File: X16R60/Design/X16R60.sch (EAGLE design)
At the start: 64 parts, among them J1 SMD Grove, K1 SMD Button Top, P1 HEXABIT__LED_MATRIX, Q1 2N7002, Q2 2N7002, SW1 LSM7-644C, U1 STM32F103C8T6, U2 XC6206P332MR, X2 8MHz

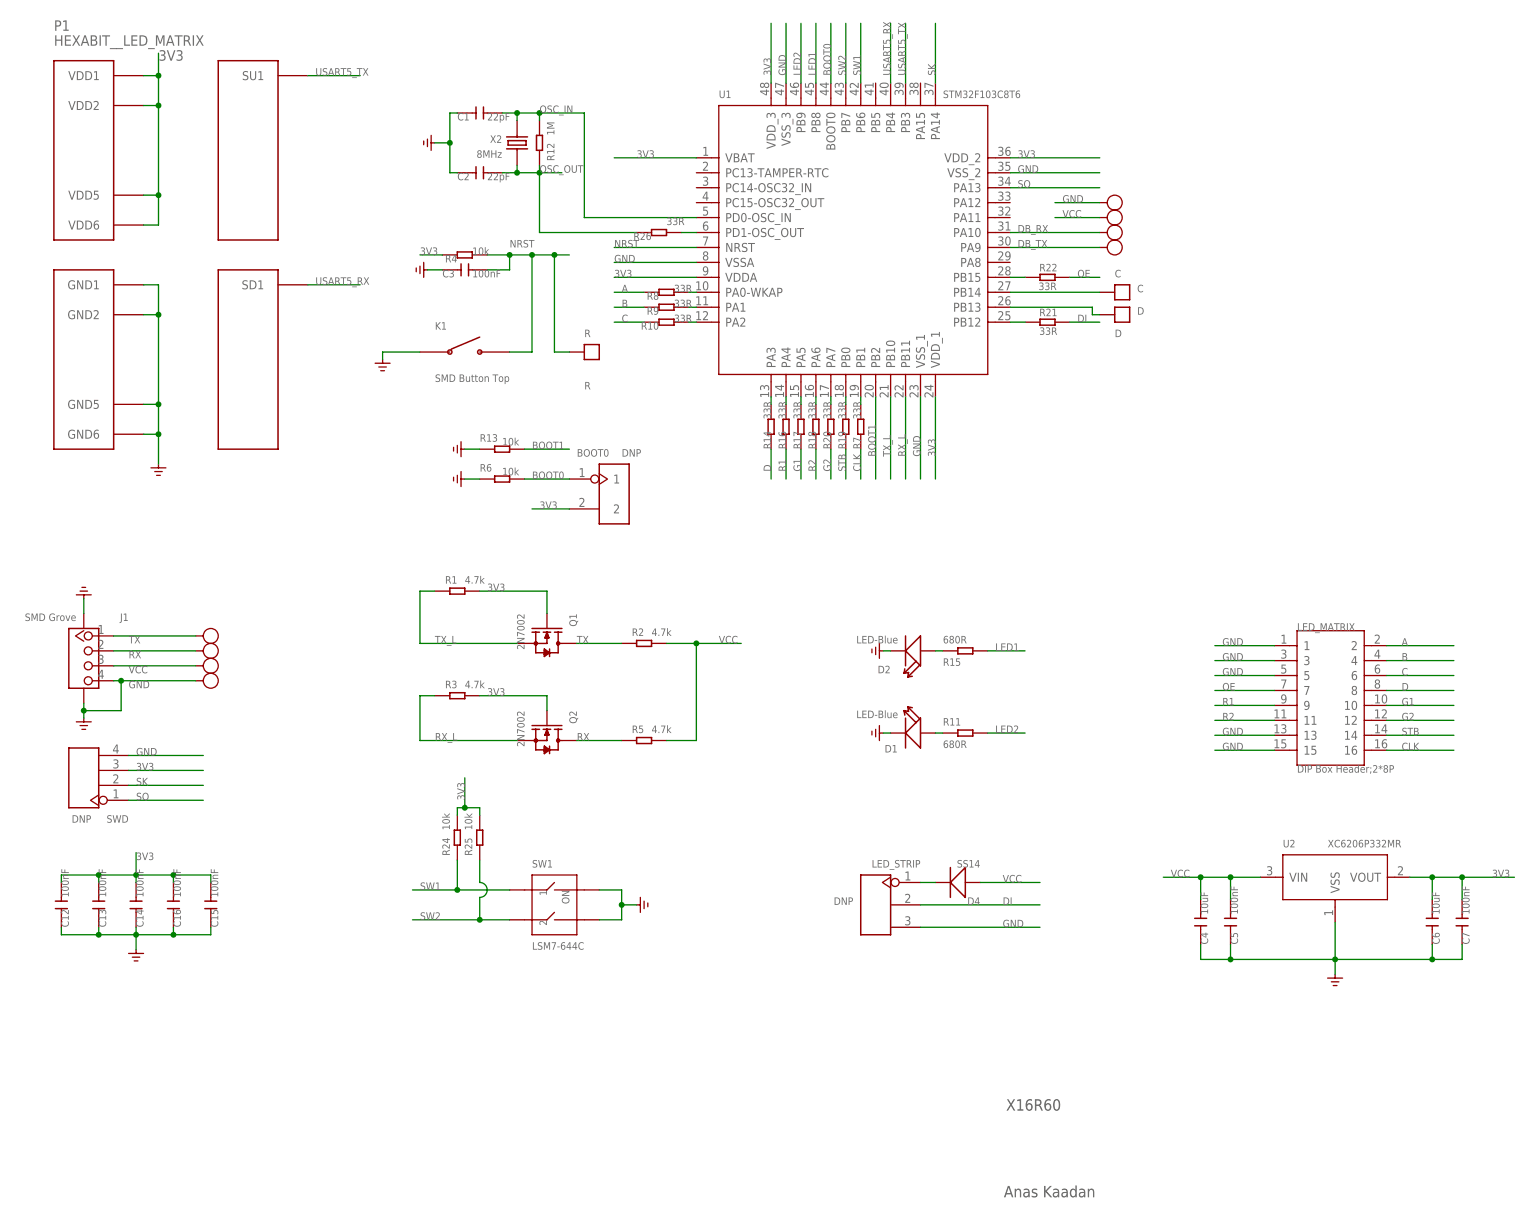
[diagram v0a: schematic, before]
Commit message: - Changed MCU.. - Deleted unnecessary components.. - Regenerated output files.. - Updated BOM.. - Updated Batch_4_21 on google docs..
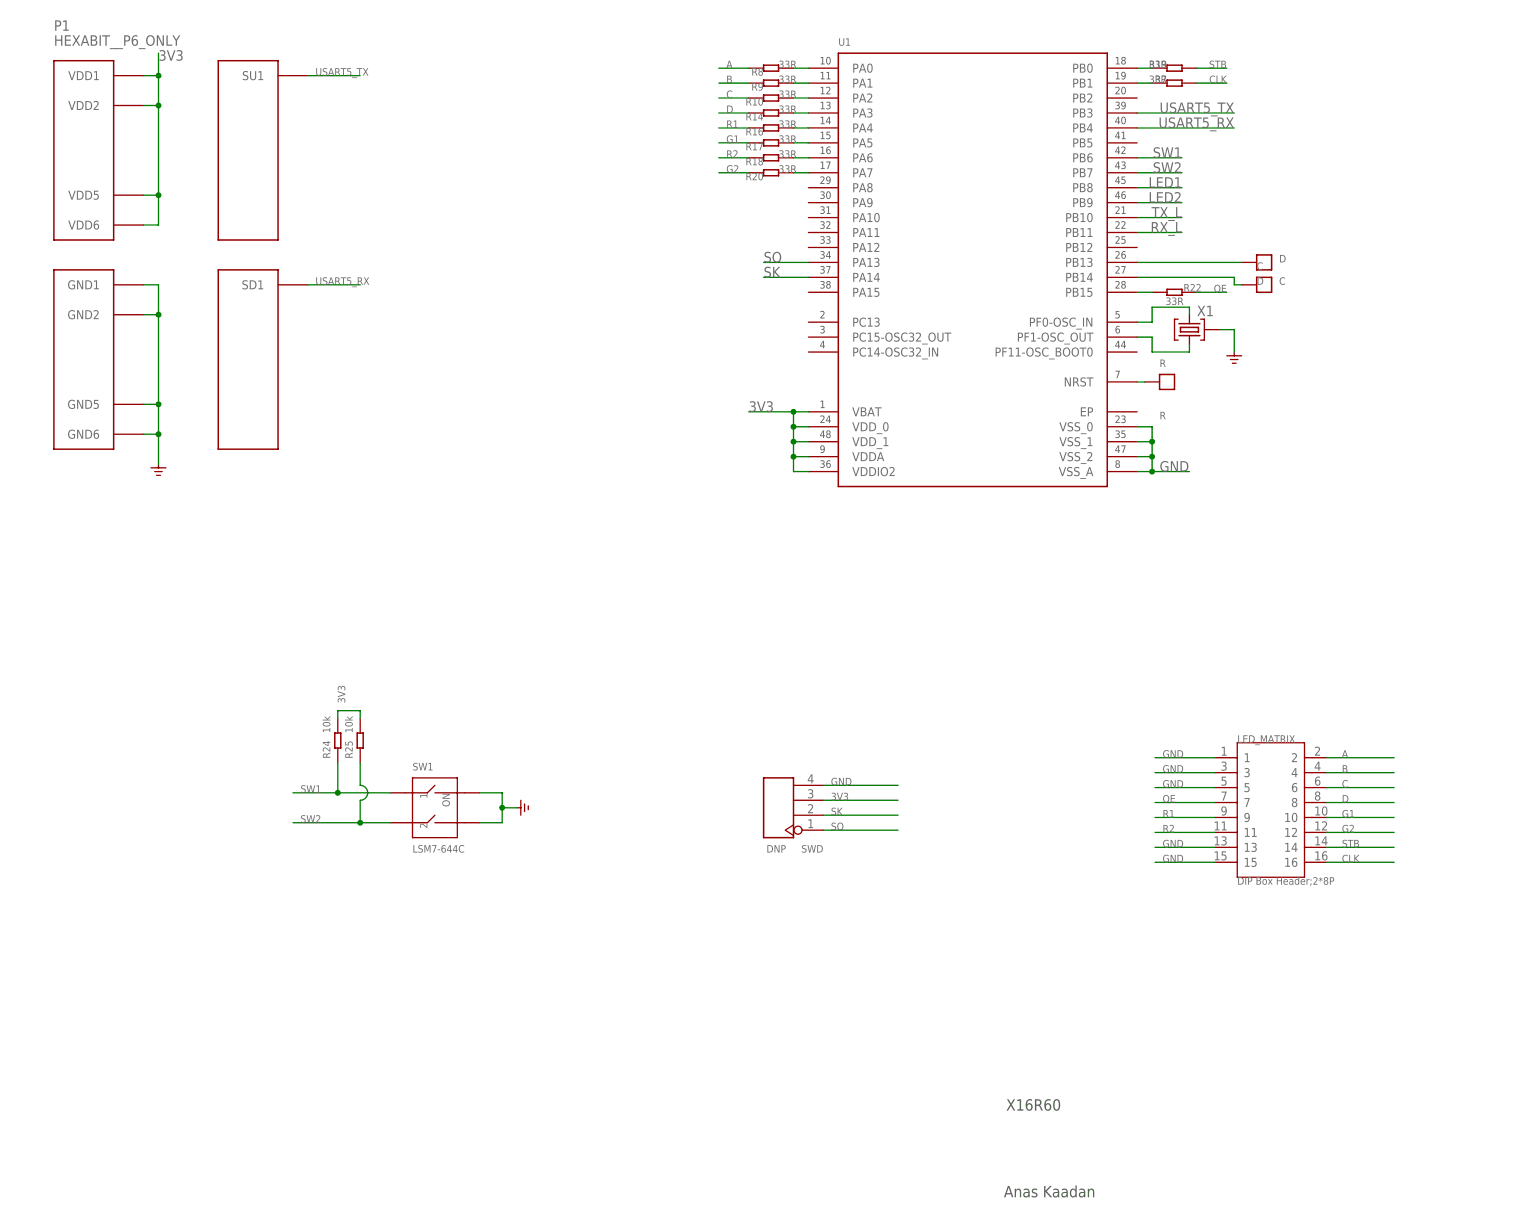
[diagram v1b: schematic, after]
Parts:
- removed BOOT0: DNP, Connector-new:HEADER-2P-1.5
- removed C1, C2: 22pF, Discrete-new:CAP-0402
- removed C12, C13, C14, C15, C16, C3, C5, C7: 100nF, Discrete-new:CAP-0402
- removed C4, C6: 10uF, Discrete-new:CAP-0402
- removed D1, D2: LED-Blue, Discrete-new:LED-0402
- removed D4: SS14, Discrete-new:DIODE'SMA'
- removed DB_RX, RX: RX, Discrete-new:TEST-POINT'4545'
- removed DB_TX, TX: TX, Discrete-new:TEST-POINT'4545'
- removed GND, GND13: GND, Discrete-new:TEST-POINT'4545'
- removed J1: SMD Grove, Connector-new:GROVE-CONNECTOR-SMD'90D'
- removed K1: SMD Button Top, Discrete-new:BUTTON-2P-SMD
- removed LED_STRIP: DNP, Connector-new:HEADER-3P-2.54
- removed Q1, Q2: 2N7002, Discrete-new:MOSFET-N'SOT23'
- removed R1, R2, R3, R5: 4.7k, Discrete-new:RES-0402
- removed R11, R15: 680R, Discrete-new:RES-0402
- removed R12: 1M, Discrete-new:RES-0402
- removed R13, R4, R6: 10k, Discrete-new:RES-0402
- removed R21, R26: 33R, Discrete-new:RES-0402
- removed U2: XC6206P332MR, IC-new:PMIC-XC6206PMR
- removed VCC, VCC1: VCC, Discrete-new:TEST-POINT'4545'
- removed X2: 8MHz, Discrete-new:CRYSTAL-2P'5032'
- added X1: (no value), HEXABITZ_OTHER_PARTS:XTALL_CSTCE8M00G52
- P1: value HEXABIT__LED_MATRIX -> HEXABIT__P6_ONLY; device hexabitz_connectors:HEXABIT__LED_MATRIX -> hexabitz_connectors:HEXABIT__P6_ONLY
- U1: value STM32F103C8T6 -> (none); device IC-new:MCU-STM32F103CBT6 -> HEXABITZ_ICs:STM32F091CBU6; DESCRIPTION ARM Cortex-M3 STM32 F1 Microcontroller 32-Bit 72MHz 64kB FL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 -> (none); MFN STMicroelectronics -> (none); MPN STM32F103C8T6 -> (none); OCTOPART_URL https://octopart.com/stm32f103c8t6-stmicroelectronics-41858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 -> (none)
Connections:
- removed net BOOT0: BOOT0.1, R6.2, U1.BOOT0
- removed net BOOT1: R13.2, U1.PB2
- removed net DB_RX: DB_RX.T, U1.PA10
- removed net DB_TX: DB_TX.T, U1.PA9
- removed net DI: LED_STRIP.P$2, R21.2
- removed net N$15 (its old number): R21.1, U1.PB12
- removed net N$16: R26.2, U1.PD1-OSC_OUT
- removed net N$17: D4.-, LED_STRIP.P$1
- removed net OSC_IN: C1.2, R12.2, U1.PD0-OSC_IN, X2.2
- removed net OSC_OUT: C2.2, R12.1, R26.1, X2.1
- removed net RX: J1.2, Q2.D, R5.1, RX.T
- removed net TX: J1.1, Q1.D, R2.1, TX.T
- removed net VCC: C4.2, C5.2, D4.+, J1.3, R2.2, R5.2, U2.VIN, VCC.T, VCC1.T
- net 3V3: now also U1.VDDIO2, U1.VDD_0; no longer BOOT0.2, C12.2, C13.2, C14.2, C15.2, C16.2, C6.2, C7.2, Q1.G, Q2.G, R1.2, R3.2, R4.1, U1.VDD_2, U1.VDD_3, U2.VOUT
- net GND: now also U1.VSS_0, U1.VSS_A, X1.2; no longer C1.1, C12.1, C13.1, C14.1, C15.1, C16.1, C2.1, C3.1, C4.1, C5.1, C6.1, C7.1, D1.-, D2.-, GND.T, GND13.T, J1.4, J1.SS1, J1.SS2, K1.1, LED_STRIP.P$3, R13.1, R6.1, U1.VSSA, U1.VSS_3, U2.VSS
- net LED1: no longer R15.2
- net LED2: no longer R11.2
- net N$1: now also U1.PF0-OSC_IN, X1.3; no longer D1.+, R11.1
- net N$3: now also U1.PA0; no longer U1.PA0-WKAP
- net N$4: now also U1.PF1-OSC_OUT, X1.1; no longer D2.+, R15.1
- net NRST: no longer C3.2, K1.2, R4.2
- net RX_L: no longer Q2.S, R3.1
- net TX_L: no longer Q1.S, R1.1
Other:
- note removed: "D1"
- moved on the sheet: C, D, LED_MATRIX, R, R10, R14, R16, R17, R18, R19, R20, R22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

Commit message: Final..
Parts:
- added B: PAD1, Hexabitz:PAD1
- added C1: 10nF, Hexabitz:C-0603
- added C2: 1.00uF, Hexabitz:C-0805-POL
- added C3, C5, C6, C8, C9: 100nF, Hexabitz:C-0603
- added C4, C7: 4.7uF, Hexabitz:C-0805-POL
- added D1: VLMS1300-GS08, Hexabitz:VLMS1300-GS08
- added FB1: FB-TDK_MMZ1608Y300B, Hexabitz:FB-TDK_MMZ1608Y300B
- added R2: 10.0K, Hexabitz:R-0603
- added R3: 270.0R, Hexabitz:R-0603
- added R4: 0.0R, Hexabitz:R-0603
- R: value R -> PAD1
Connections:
- removed net 3V3: P1.VDD1, P1.VDD2, P1.VDD5, P1.VDD6, R24.2, R25.2, SWD.P$3, U1.VBAT, U1.VDDA, U1.VDDIO2, U1.VDD_0, U1.VDD_1
- removed net NRST: R.P$1, U1.NRST
- new net B1: B.P$1, R2.2, U1.PF11-OSC_BOOT0
- new net N$14: D1.A, R3.1
- new net N$16: R3.2, U1.PA11
- new net R3: C8.1, R.P$1, U1.NRST
- new net VDD: C3.1, C4.+, C5.1, C6.1, C7.+, C9.1, FB1.2, P1.VDD1, P1.VDD2, P1.VDD5, P1.VDD6, R24.2, R25.2, SWD.P$3, U1.VBAT, U1.VDDIO2, U1.VDD_0, U1.VDD_1
- new net VDDA: C1.1, C2.+, FB1.1, U1.VDDA
- new net VSSA: C1.2, C2.-, R4.2, U1.VSS_A
- net GND: now also C3.2, C4.-, C5.2, C6.2, C7.-, C8.2, C9.2, D1.C, R2.1, R4.1, U1.EP; no longer U1.VSS_A
- net N$1: now also X1.1; no longer X1.3
- net N$4: now also X1.3; no longer X1.1
- net SW1: now also R25.1, SW1.2; no longer R24.1, SW1.1
- net SW2: now also R24.1, SW1.1; no longer R25.1, SW1.2
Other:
- note added: "VBAT"
- note added: "VDD Coupling"
- note added: "VDD=3.3 Volts"
- note added: "VDDA Coupling"
- note added: "VDDIO2 Coupling"
- moved on the sheet: LED_MATRIX, P1, R, R24, R25, SW1, SWD, X1
